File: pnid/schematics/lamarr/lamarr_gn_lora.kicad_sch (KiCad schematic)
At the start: 16 parts

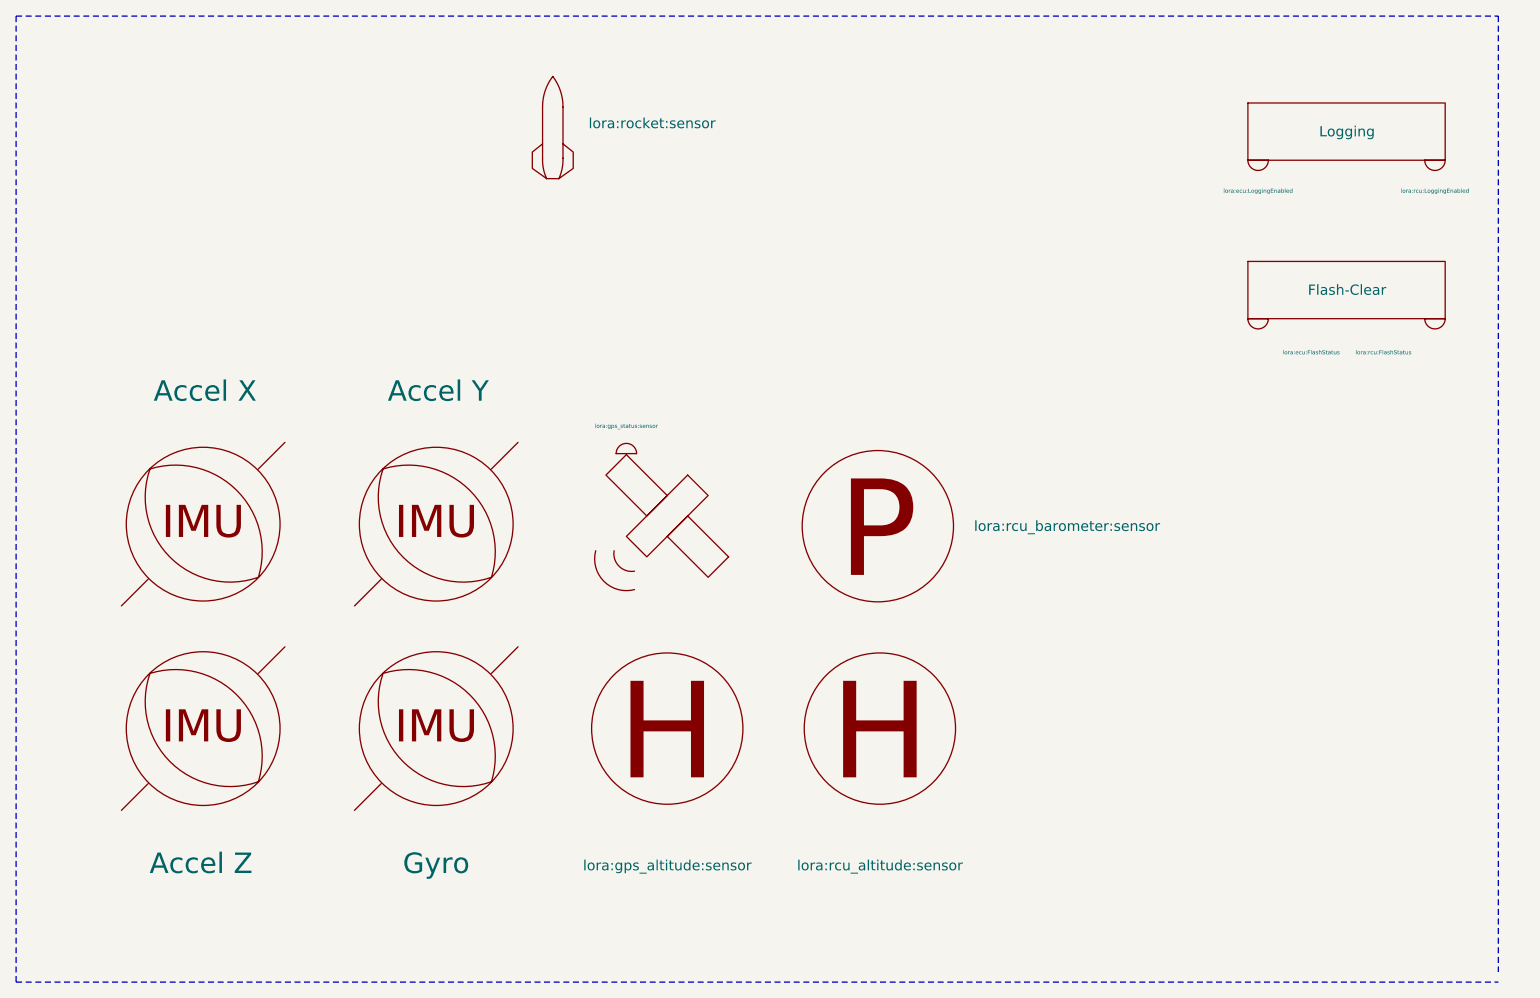
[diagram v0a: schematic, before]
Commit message: various fixes
configure lora use,
fix guidance & navigation pnid,
fix retract threshold
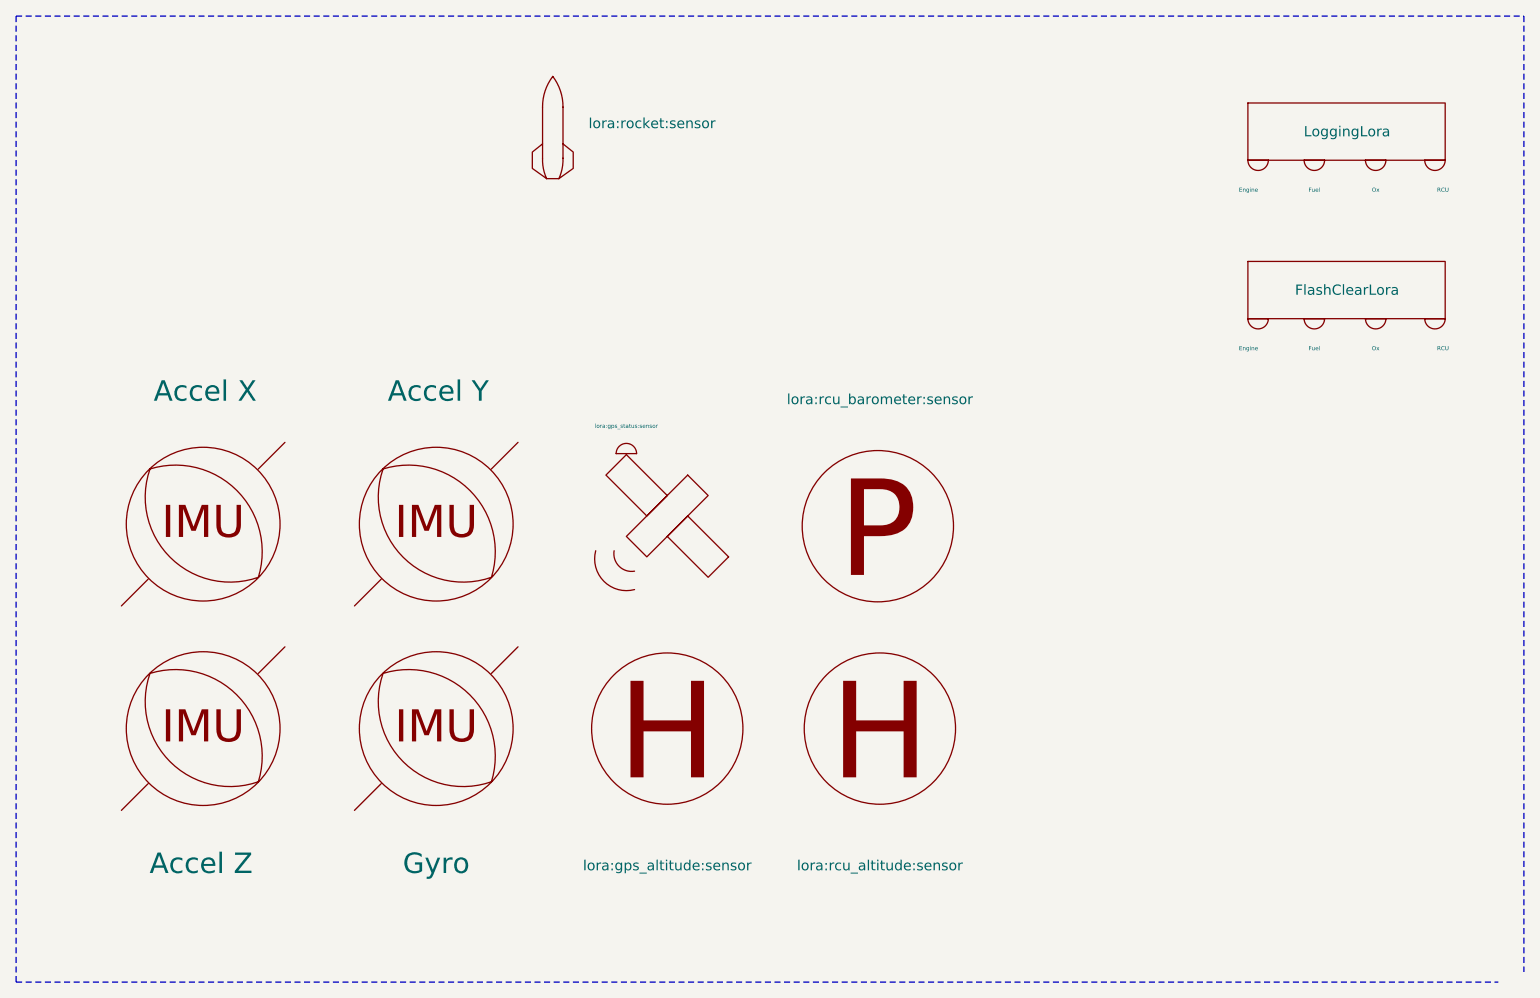
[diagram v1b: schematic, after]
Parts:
- removed ecu_flash_status: lora:ecu:FlashStatus, symbol PnID-Lib:LED
- removed ecu_logging_en: lora:ecu:LoggingEnabled, symbol PnID-Lib:LED
- removed rcu_flash_status: lora:rcu:FlashStatus, symbol PnID-Lib:LED
- removed rcu_logging_en: lora:rcu:LoggingEnabled, symbol PnID-Lib:LED
- added Engine: engine_ecu:LoggingEnabled, symbol PnID-Lib:LED
- added Engine: engine_ecu:FlashStatus, symbol PnID-Lib:LED
- added Fuel: fuel_ecu:LoggingEnabled, symbol PnID-Lib:LED
- added Fuel: fuel_ecu:FlashStatus, symbol PnID-Lib:LED
- added Ox: ox_ecu:LoggingEnabled, symbol PnID-Lib:LED
- added Ox: ox_ecu:FlashStatus, symbol PnID-Lib:LED
- added RCU: rcu:FlashStatus, symbol PnID-Lib:LED
- added RCU: rcu:LoggingEnabled, symbol PnID-Lib:LED
- Logging: value Logging -> LoggingLora
- Logging?: value Flash-Clear -> FlashClearLora
- gnss: value GNSS -> GNSSLora
